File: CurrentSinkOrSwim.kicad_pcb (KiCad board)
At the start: 2 copper layers, 41.7 x 50.8 mm, 22 parts, among them P101 CONN_01X03, P102 CONN_01X02, P103 CONN_01X02, P201 CONN_01X01, Q201 BUK9575, U201 LMV358, U401 LM2931D-R

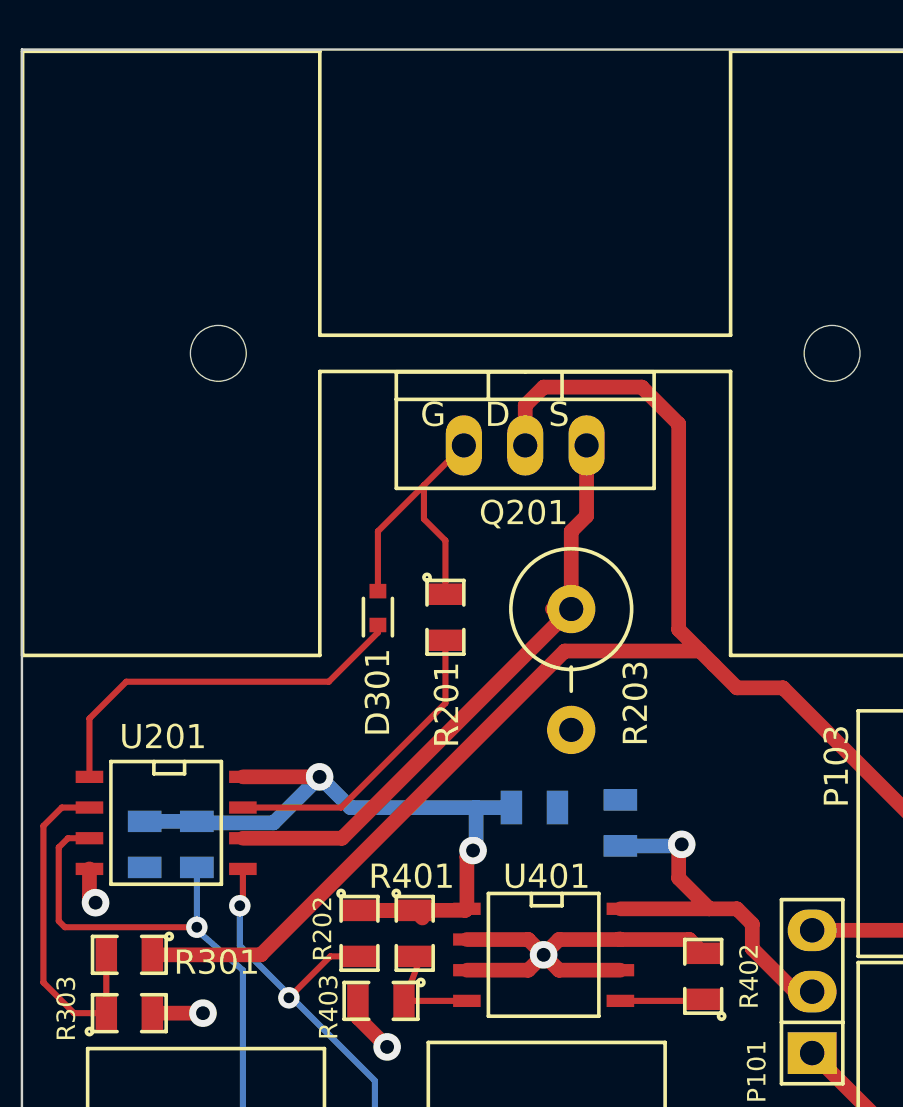
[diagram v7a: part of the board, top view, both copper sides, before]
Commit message: Added logo and fixed 3d view
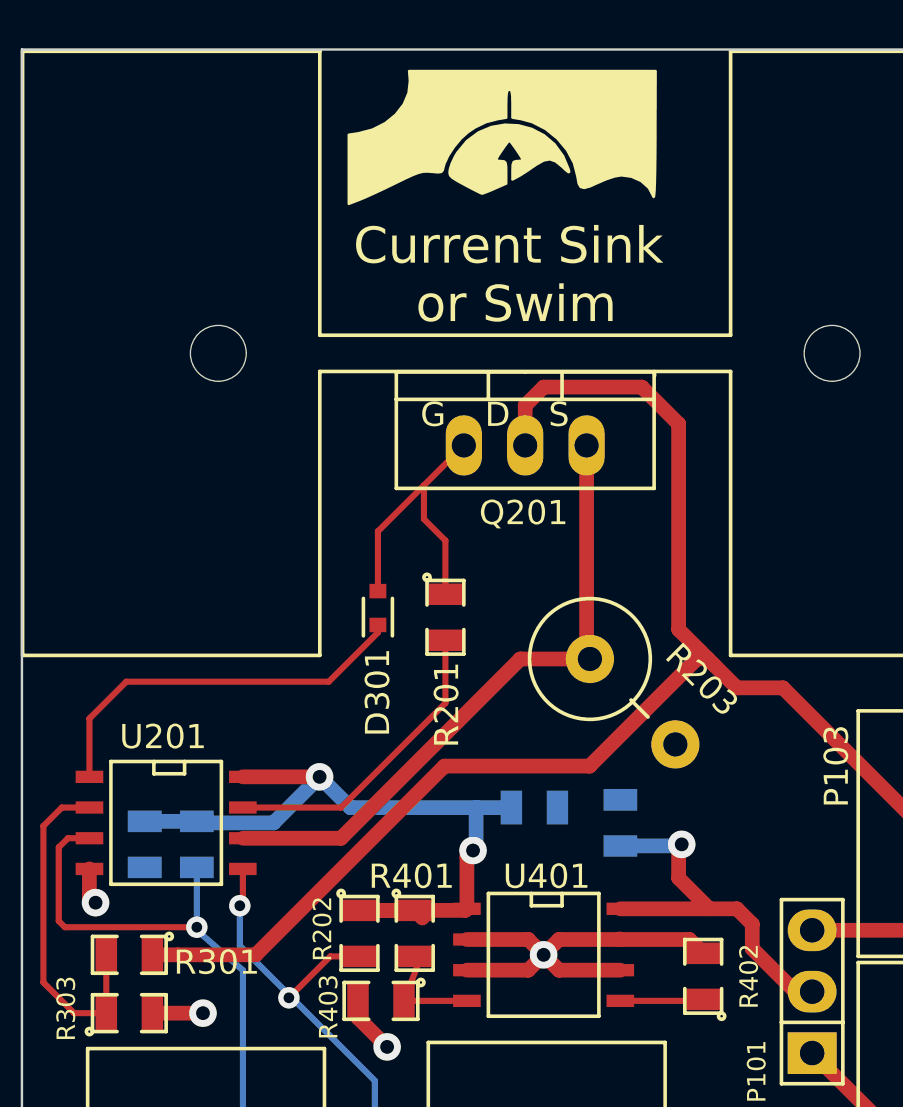
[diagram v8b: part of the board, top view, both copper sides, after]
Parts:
- added G***: LOGO, CSOS Local:csos-logo, F.Cu at (115.9, 49.3)
- moved R203 2.87 mm to (121.3, 69.0), turned to 315 degrees
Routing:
- net Net-(Q201-PadS): track 25.3 -> 26.3 mm
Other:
- board text added: "Current Sink or Swim"
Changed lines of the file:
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@@
     (links 42)
     (no_connects 0)
-    (area 95.961999 41.986999 137.718001 92.887001)
+    (area 95.660199 41.730199 142.373134 98.660801)
     (thickness 1.6)
-    (drawings 4)
-    (tracks 133)
+    (drawings 5)
+    (tracks 136)
     (zones 0)
-    (modules 22)
+    (modules 23)
     (nets 17)
   )
@@
       (drillshape 1)
       (scaleselection 1)
-      (outputdirectory ""))
+      (outputdirectory image/))
   )
   (net 0 "")
@@
   )
   (module Resistors_ThroughHole:Resistor_Vertical_RM5mm (layer F.Cu)
-    (at 118.745 67.691 270)
+    (at 121.285 69.0245 315)
     (descr "Resistor, Vertical, RM 5mm, 1/3W,")
     (tags "Resistor, Vertical, RM 5mm, 1/3W,")
-    (fp_text reference R203 (at 1.397 -2.667 270) (layer F.SilkS)
-      (effects (font (size 1 1) (thickness 0.15)))
-    )
-    (fp_text value .1 (at 0 4.50088 270) (layer F.SilkS) hide
+    (fp_text reference R203 (at 1.397 -2.667 315) (layer F.SilkS)
+      (effects (font (size 1 1) (thickness 0.15)))
+    )
+    (fp_text value .1 (at 0 4.50088 315) (layer F.SilkS) hide
       (effects (font (size 1 1) (thickness 0.15)))
     )
     (fp_line (start -0.09906 0) (end 0.9017 0) (layer F.SilkS) (width 0.15))
     (fp_circle (center -2.49936 0) (end 0 0) (layer F.SilkS) (width 0.15))
-    (pad 1 thru_hole circle (at -2.49936 0 270) (size 1.99898 1.99898) (drill 1.00076) (layers *.Cu *.SilkS *.Mask)
+    (pad 1 thru_hole circle (at -2.49936 0 315) (size 1.99898 1.99898) (drill 1.00076) (layers *.Cu *.SilkS *.Mask)
       (net 8 "Net-(Q201-PadS)"))
-    (pad 2 thru_hole circle (at 2.5019 0 270) (size 1.99898 1.99898) (drill 1.00076) (layers *.Cu *.SilkS *.Mask)
-      (net 2 GND))
+    (pad 2 thru_hole circle (at 2.5019 0 315) (size 1.99898 1.99898) (drill 1.00076) (layers *.Cu *.SilkS *.Mask)
+      (net 2 GND))
+  )
+  (module "CSOS Local:csos-logo" (layer F.Cu)
+    (at 115.8875 49.276)
+    (fp_text reference G*** (at 0 0) (layer F.SilkS) hide
+      (effects (font (thickness 0.3)))
+    )
+    (fp_text value LOGO (at 0.75 0) (layer F.SilkS) hide
+      (effects (font (thickness 0.3)))
+    )
+    (fp_poly (pts (xy 6.332589 6.248175) (xy 6.321406 6.2865) (xy 6.290503 6.297136) (xy 6.278701 6.180666)
+      (xy 6.292007 6.060471) (xy 6.321406 6.074833) (xy 6.332589 6.248175) (xy 6.332589 6.248175)) (layer F.SilkS) (width 0.1))
+    (fp_poly (pts (xy 6.35 -6.35) (xy 6.342364 -3.6195) (xy 6.338041 -2.844779) (xy 6.32992 -2.205589)
+      (xy 6.318217 -1.708474) (xy 6.30315 -1.359975) (xy 6.284937 -1.166635) (xy 6.263794 -1.134996)
+      (xy 6.260074 -1.14565) (xy 6.070103 -1.511787) (xy 5.754746 -1.796131) (xy 5.347069 -1.97661)
+      (xy 4.932164 -2.032) (xy 4.658011 -1.988116) (xy 4.293298 -1.867165) (xy 3.987667 -1.733968)
+      (xy 3.631328 -1.575223) (xy 3.393129 -1.511035) (xy 3.245805 -1.549173) (xy 3.162094 -1.697404)
+      (xy 3.114734 -1.963497) (xy 3.112456 -1.983355) (xy 2.968407 -2.545754) (xy 2.682376 -3.079807)
+      (xy 2.28171 -3.557623) (xy 1.79376 -3.95131) (xy 1.245874 -4.232976) (xy 0.783166 -4.358849)
+      (xy 0.423333 -4.417551) (xy 0.423333 -5.002776) (xy 0.415702 -5.322469) (xy 0.388292 -5.504557)
+      (xy 0.334326 -5.580271) (xy 0.296333 -5.588) (xy 0.226956 -5.552838) (xy 0.187441 -5.426531)
+      (xy 0.17101 -5.177851) (xy 0.169333 -5.002776) (xy 0.169333 -4.417551) (xy -0.181877 -4.358215)
+      (xy -0.66885 -4.233561) (xy -1.117966 -4.016975) (xy -1.41718 -3.817206) (xy -1.70709 -3.556147)
+      (xy -1.990765 -3.216269) (xy -2.230436 -2.850985) (xy -2.388332 -2.51371) (xy -2.420075 -2.398898)
+      (xy -2.458164 -2.244349) (xy -2.523351 -2.169874) (xy -2.662911 -2.154507) (xy -2.920638 -2.176926)
+      (xy -3.110434 -2.190699) (xy -3.279871 -2.181082) (xy -3.463619 -2.137161) (xy -3.696349 -2.048025)
+      (xy -4.01273 -1.90276) (xy -4.414301 -1.706803) (xy -4.843446 -1.498766) (xy -5.261431 -1.302511)
+      (xy -5.6233 -1.138746) (xy -5.884097 -1.028183) (xy -5.9055 -1.019844) (xy -6.35 -0.849138)
+      (xy -6.35 -2.282048) (xy -6.35 -3.714958) (xy -5.947834 -3.77494) (xy -5.360352 -3.928988)
+      (xy -4.839039 -4.193979) (xy -4.404201 -4.548819) (xy -4.076142 -4.972412) (xy -3.875168 -5.443665)
+      (xy -3.821583 -5.941482) (xy -3.824215 -5.981109) (xy -3.853554 -6.35) (xy 1.248223 -6.35)
+      (xy 6.35 -6.35) (xy 6.35 -6.35)) (layer F.SilkS) (width 0.1))
+    (fp_poly (pts (xy 2.775091 -2.176038) (xy 2.742605 -2.16183) (xy 2.630231 -2.252313) (xy 2.482437 -2.391834)
+      (xy 2.21545 -2.607974) (xy 1.974172 -2.69267) (xy 1.717188 -2.646432) (xy 1.40308 -2.469766)
+      (xy 1.312062 -2.406203) (xy 1.041096 -2.21941) (xy 0.78807 -2.057083) (xy 0.656166 -1.980695)
+      (xy 0.423333 -1.858319) (xy 0.423333 -2.241493) (xy 0.43199 -2.477447) (xy 0.47463 -2.589566)
+      (xy 0.576255 -2.623109) (xy 0.635 -2.624667) (xy 0.794269 -2.641222) (xy 0.846666 -2.672912)
+      (xy 0.802955 -2.764636) (xy 0.694539 -2.937779) (xy 0.555494 -3.142902) (xy 0.419898 -3.330567)
+      (xy 0.321828 -3.451336) (xy 0.296333 -3.471334) (xy 0.23311 -3.407918) (xy 0.113766 -3.250628)
+      (xy -0.02762 -3.048903) (xy -0.156974 -2.852181) (xy -0.240217 -2.7099) (xy -0.254 -2.672912)
+      (xy -0.181368 -2.63661) (xy -0.042334 -2.624667) (xy 0.078788 -2.612616) (xy 0.141917 -2.548868)
+      (xy 0.165826 -2.392029) (xy 0.169333 -2.157933) (xy 0.169333 -1.691199) (xy -0.306869 -1.4806)
+      (xy -0.565549 -1.370487) (xy -0.758831 -1.296161) (xy -0.836036 -1.275016) (xy -0.92966 -1.314833)
+      (xy -1.134919 -1.41701) (xy -1.414766 -1.562867) (xy -1.549709 -1.634849) (xy -1.864404 -1.806722)
+      (xy -2.056537 -1.927468) (xy -2.15326 -2.025087) (xy -2.18172 -2.127575) (xy -2.169067 -2.262932)
+      (xy -2.16768 -2.272141) (xy -2.096935 -2.50413) (xy -1.961875 -2.792888) (xy -1.858991 -2.969062)
+      (xy -1.45672 -3.456743) (xy -0.978768 -3.810553) (xy -0.448509 -4.033954) (xy 0.110679 -4.130411)
+      (xy 0.67542 -4.103388) (xy 1.222338 -3.95635) (xy 1.728057 -3.692761) (xy 2.1692 -3.316084)
+      (xy 2.522392 -2.829784) (xy 2.75031 -2.286) (xy 2.775091 -2.176038) (xy 2.775091 -2.176038)) (layer F.SilkS) (width 0.1))
+  )
+  (gr_text "Current Sink\n or Swim" (at 116.1415 51.3715) (layer F.SilkS)
+    (effects (font (size 1.5 1.5) (thickness 0.3)))
   )
   (gr_line (start 137.668 42.037) (end 137.668 92.837) (angle 90) (layer Edge.Cuts) (width 0.1))
@@
   (segment (start 134.62 87.4395) (end 132.588 87.4395) (width 0.6096) (layer F.Cu) (net 6))
   (segment (start 132.588 87.4395) (end 128.7145 83.566) (width 0.6096) (layer F.Cu) (net 6))
+  (segment (start 123.94946 67.24904) (end 119.507 71.6915) (width 0.6096) (layer F.Cu) (net 7))
+  (segment (start 102.4636 79.502) (end 101.4095 79.502) (width 0.6096) (layer F.Cu) (net 7))
+  (segment (start 119.507 71.6915) (end 113.49767 71.6915) (width 0.6096) (layer F.Cu) (net 7))
+  (segment (start 113.49767 71.6915) (end 105.68717 79.502) (width 0.6096) (layer F.Cu) (net 7))
+  (segment (start 105.68717 79.502) (end 102.4636 79.502) (width 0.6096) (layer F.Cu) (net 7))
+  (segment (start 124.39904 67.24904) (end 124.079 66.929) (width 0.6096) (layer F.Cu) (net 7))
+  (segment (start 124.6378 67.4878) (end 124.39904 67.24904) (width 0.6096) (layer F.Cu) (net 7))
+  (segment (start 124.39904 67.24904) (end 123.94946 67.24904) (width 0.6096) (layer F.Cu) (net 7))
   (segment (start 128.7145 78.486) (end 133.1595 78.486) (width 0.6096) (layer F.Cu) (net 7))
   (segment (start 133.1595 78.486) (end 134.62 77.0255) (width 0.6096) (layer F.Cu) (net 7))
-  (segment (start 101.4095 79.502) (end 105.900218 79.502) (width 0.6096) (layer F.Cu) (net 7))
-  (segment (start 105.900218 79.502) (end 118.473218 66.929) (width 0.6096) (layer F.Cu) (net 7))
-  (segment (start 118.473218 66.929) (end 124.079 66.929) (width 0.6096) (layer F.Cu) (net 7))
   (segment (start 134.62 75.565) (end 127.508 68.453) (width 0.6096) (layer F.Cu) (net 7))
   (segment (start 127.508 68.453) (end 125.603 68.453) (width 0.6096) (layer F.Cu) (net 7))
-  (segment (start 124.6378 67.4878) (end 124.079 66.929) (width 0.6096) (layer F.Cu) (net 7))
   (segment (start 124.079 66.929) (end 123.19 66.04) (width 0.6096) (layer F.Cu) (net 7))
   (segment (start 125.603 68.453) (end 124.6378 67.4878) (width 0.6096) (layer F.Cu) (net 7))
@@
   (segment (start 116.84 56.769) (end 116.84 58.42) (width 0.6096) (layer F.Cu) (net 7))
   (segment (start 134.62 77.0255) (end 134.62 75.565) (width 0.6096) (layer F.Cu) (net 7))
-  (segment (start 105.156 74.676) (end 109.26064 74.676) (width 0.6096) (layer F.Cu) (net 8))
-  (segment (start 109.26064 74.676) (end 118.745 65.19164) (width 0.6096) (layer F.Cu) (net 8))
-  (segment (start 118.745 65.19164) (end 118.745 61.976) (width 0.6096) (layer F.Cu) (net 8))
-  (segment (start 119.38 61.341) (end 119.38 58.42) (width 0.6096) (layer F.Cu) (net 8))
-  (segment (start 118.745 61.976) (end 119.38 61.341) (width 0.6096) (layer F.Cu) (net 8))
-  (segment (start 118.745 65.19164) (end 117.96776 65.19164) (width 0.6096) (layer F.Cu) (net 8))
+  (segment (start 119.517686 67.257186) (end 116.638814 67.257186) (width 0.6096) (layer F.Cu) (net 8))
+  (segment (start 109.22 74.676) (end 105.156 74.676) (width 0.6096) (layer F.Cu) (net 8))
+  (segment (start 116.638814 67.257186) (end 109.22 74.676) (width 0.6096) (layer F.Cu) (net 8))
+  (segment (start 119.38 58.42) (end 119.38 67.1195) (width 0.6096) (layer F.Cu) (net 8))
+  (segment (start 119.38 67.1195) (end 119.517686 67.257186) (width 0.6096) (layer F.Cu) (net 8))
   (segment (start 105.156 73.406) (end 109.22 73.406) (width 0.254) (layer F.Cu) (net 9))
   (segment (start 113.538 69.088) (end 113.538 66.4845) (width 0.254) (layer F.Cu) (net 9))
